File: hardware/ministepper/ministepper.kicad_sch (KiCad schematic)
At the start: 9 parts, among them U1 STM32G071G8U6, U4 SIT3088EEUA

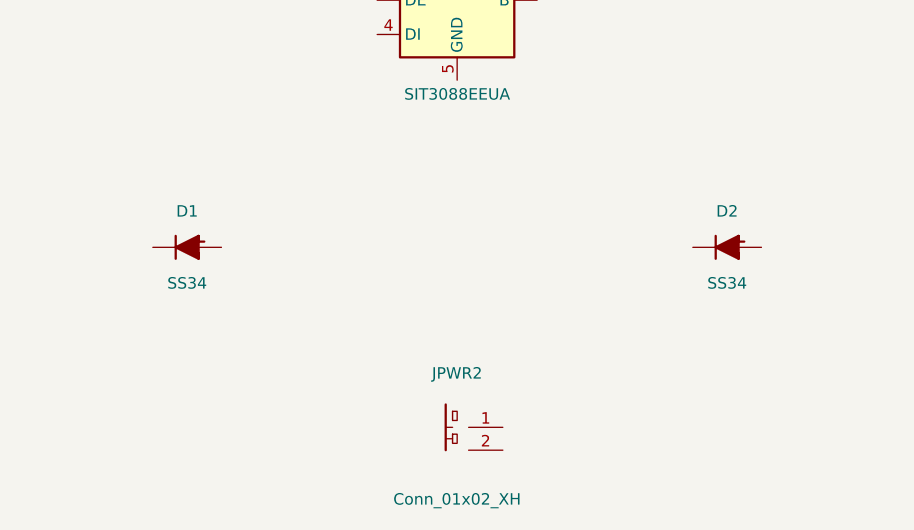
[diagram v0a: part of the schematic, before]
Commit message: hw/ministepper: upgrade D1/D2 SS34 (3A) -> SS54 (5A)
Two TMC2130 drivers at 1.4A continuous each plus chopper peaks and
startup inrush can exceed the SS34's 3A rating on the motor-supply
OR path. SS54 is a drop-in (same SMA footprint, same 40V rating,
JLCPCB basic part C22452) with 5A continuous headroom.

Co-Authored-By: Claude Opus 4.6 (1M context) <noreply@anthropic.com>
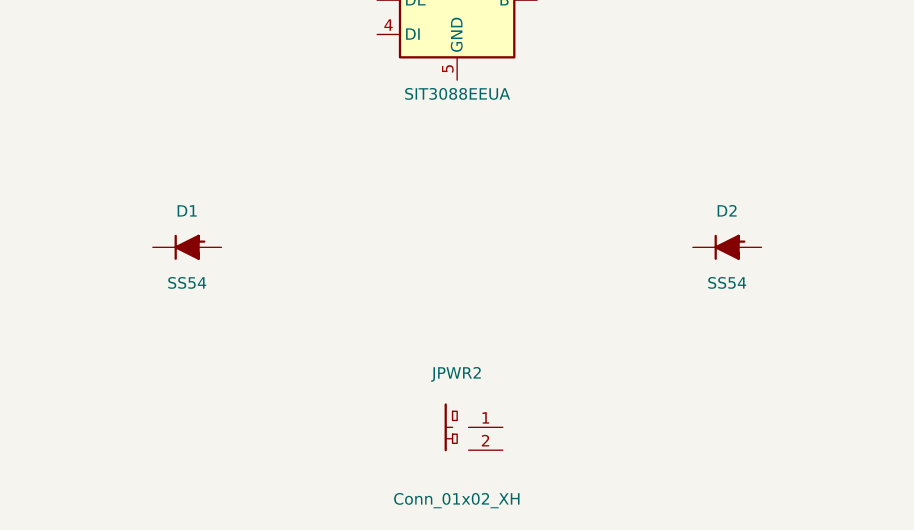
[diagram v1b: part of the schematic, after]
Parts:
- D1, D2: value SS34 -> SS54; LCSC C8678 -> C22452; MPN SS34 -> SS54
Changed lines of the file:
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@@
 			)
 		)
-		(property "Value" "SS34"
+		(property "Value" "SS54"
 			(at 120 214 0)
 			(show_name no)
@@
 			)
 		)
-		(property "Description" "Schottky 3A 40V SMA — reverse-polarity + diode-OR for external motor input (BASIC)"
+		(property "Description" "Schottky 5A 40V SMA — reverse-polarity + diode-OR for external motor input (BASIC)"
 			(at 120 210 0)
 			(hide yes)
@@
 			)
 		)
-		(property "LCSC" "C8678"
+		(property "LCSC" "C22452"
 			(at 120 210 0)
 			(hide yes)
@@
 			)
 		)
-		(property "MPN" "SS34"
+		(property "MPN" "SS54"
 			(at 120 210 0)
 			(hide yes)
@@
 			)
 		)
-		(property "Value" "SS34"
+		(property "Value" "SS54"
 			(at 180 214 0)
 			(show_name no)
@@
 			)
 		)
-		(property "Description" "Schottky 3A 40V SMA — diode-OR from bus V+ onto VPP (BASIC)"
+		(property "Description" "Schottky 5A 40V SMA — diode-OR from bus V+ onto VPP (BASIC)"
 			(at 180 210 0)
 			(hide yes)
@@
 			)
 		)
-		(property "LCSC" "C8678"
+		(property "LCSC" "C22452"
 			(at 180 210 0)
 			(hide yes)
@@
 			)
 		)
-		(property "MPN" "SS34"
+		(property "MPN" "SS54"
 			(at 180 210 0)
 			(hide yes)

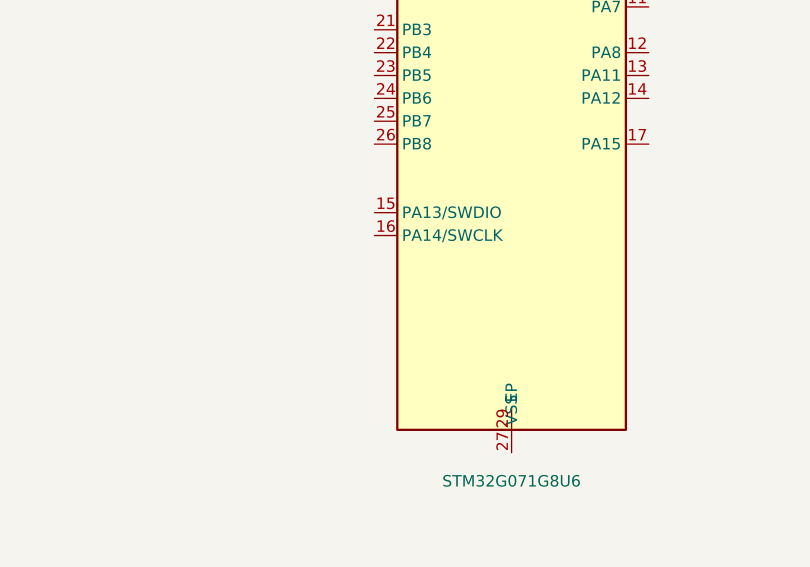
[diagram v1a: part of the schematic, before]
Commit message: hw/ministepper: add BOOT0 pull-down + test pad for bootloader entry
PA14 doubles as SWCLK and the BOOT0 selector (factory default
nBOOT_SEL=1 reads BOOT0 from the pin). Without a pull, PA14 can float
to indeterminate state at cold boot when no debugger is attached and
cause an unintended system-bootloader entry.

- R_BOOT0 (10k 0402, C25744) — locks BOOT0 low at power-up; weak
  enough not to fight SWD drive levels during debug.
- TP_BOOT0 (1x1mm solder pad) — tweezer/pogo to +3V3 at reset to
  invoke the system bootloader over USART2 (RS-485), I2C1 (PB6/PB7),
  or SPI1.

Also embedded Device:R and Connector:TestPoint in lib_symbols so
kicad-cli BOM export recognizes them.

Co-Authored-By: Claude Opus 4.6 (1M context) <noreply@anthropic.com>
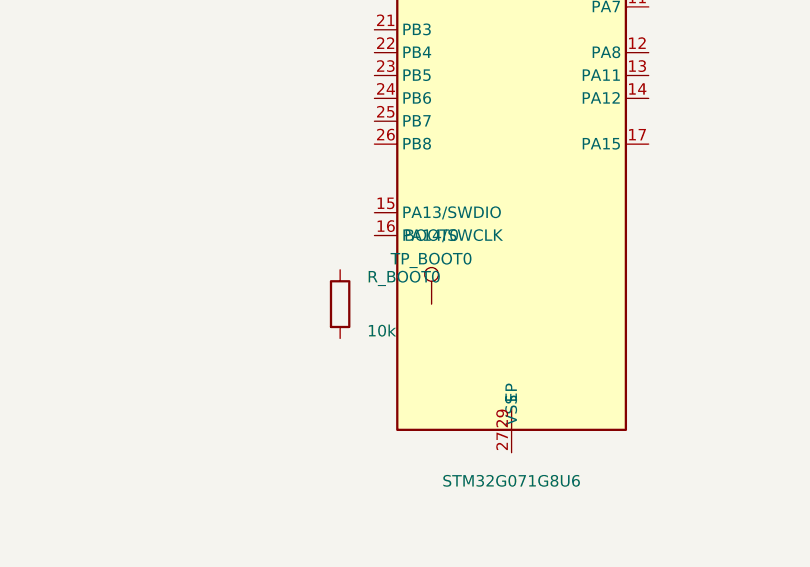
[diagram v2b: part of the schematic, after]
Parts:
- added R_BOOT0: 10k, Resistor_SMD:R_0402_1005Metric, symbol Device:R
- added TP_BOOT0: BOOT0, TestPoint:TestPoint_Pad_1.0x1.0mm, symbol Connector:TestPoint
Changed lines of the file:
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@@
+		)
+	)
+	(symbol
+		(lib_id "Device:R")
+		(at 200.66 134.62 0)
+		(unit 1)
+		(body_style 1)
+		(exclude_from_sim no)
+		(in_bom yes)
+		(on_board yes)
+		(in_pos_files yes)
+		(dnp no)
+		(uuid "b007aa01-1111-2222-3333-00000000r1ab")
+		(property "Reference" "R_BOOT0"
+			(at 203.66 131.62 0)
+			(show_name no)
+			(do_not_autoplace no)
+			(effects
+				(font
+					(size 1.27 1.27)
+				)
+				(justify left)
+			)
+		)
+		(property "Value" "10k"
+			(at 203.66 137.62 0)
+			(show_name no)
+			(do_not_autoplace no)
+			(effects
+				(font
+					(size 1.27 1.27)
+				)
+				(justify left)
+			)
+		)
+		(property "Footprint" "Resistor_SMD:R_0402_1005Metric"
+			(at 200.66 134.62 0)
+			(hide yes)
+			(show_name no)
+			(do_not_autoplace no)
+			(effects
+				(font
+					(size 1.27 1.27)
+				)
+			)
+		)
+		(property "Datasheet" ""
+			(at 200.66 134.62 0)
+			(hide yes)
+			(show_name no)
+			(do_not_autoplace no)
+			(effects
+				(font
+					(size 1.27 1.27)
+				)
+			)
+		)
+		(property "Description" "BOOT0 pull-down on PA14; locks cold boot to flash (BASIC)"
+			(at 200.66 134.62 0)
+			(hide yes)
+			(show_name no)
+			(do_not_autoplace no)
+			(effects
+				(font
+					(size 1.27 1.27)
+				)
+			)
+		)
+		(property "LCSC" "C25744"
+			(at 200.66 134.62 0)
+			(hide yes)
+			(show_name no)
+			(do_not_autoplace no)
+			(effects
+				(font
+					(size 1.27 1.27)
+				)
+			)
+		)
+		(property "MPN" "0402WGF1002TCE"
+			(at 200.66 134.62 0)
+			(hide yes)
+			(show_name no)
+			(do_not_autoplace no)
+			(effects
+				(font
+					(size 1.27 1.27)
+				)
+			)
+		)
+		(property "Manufacturer" "UNI-ROYAL"
+			(at 200.66 134.62 0)
+			(hide yes)
+			(show_name no)
+			(do_not_autoplace no)
+			(effects
+				(font
+					(size 1.27 1.27)
+				)
+			)
+		)
+		(pin "1"
+			(uuid "b007aa01-1111-2222-3333-00000000-pn01")
+		)
+		(pin "2"
+			(uuid "b007aa01-1111-2222-3333-00000000-pn02")
+		)
+		(instances
+			(project "ministepper"
+				(path "/e1d2c3b4-a5f6-7890-abcd-ef9876543210"
+					(reference "R_BOOT0")
+					(unit 1)
+				)
+			)
+		)
+	)
+	(symbol
+		(lib_id "Connector:TestPoint")
+		(at 210.82 134.62 0)
+		(unit 1)
+		(body_style 1)
+		(exclude_from_sim no)
+		(in_bom yes)
+		(on_board yes)
+		(in_pos_files yes)
+		(dnp no)
+		(uuid "b007aa02-1111-2222-3333-00000000tpab")
+		(property "Reference" "TP_BOOT0"
+			(at 210.82 129.62 0)
+			(show_name no)
+			(do_not_autoplace no)
+			(effects
+				(font
+					(size 1.27 1.27)
+				)
+			)
+		)
+		(property "Value" "BOOT0"
+			(at 210.82 127.0 0)
+			(show_name no)
+			(do_not_autoplace no)
+			(effects
+				(font
+					(size 1.27 1.27)
+				)
+			)
+		)
+		(property "Footprint" "TestPoint:TestPoint_Pad_1.0x1.0mm"
+			(at 210.82 134.62 0)
+			(hide yes)
+			(show_name no)
+			(do_not_autoplace no)
+			(effects
+				(font
+					(size 1.27 1.27)
+				)
+			)
+		)
+		(property "Datasheet" ""
+			(at 210.82 134.62 0)
+			(hide yes)
+			(show_name no)
+			(do_not_autoplace no)
+			(effects
+				(font
+					(size 1.27 1.27)
+				)
+			)
+		)
+		(property "Description" "Solder test point for manual BOOT0 select (short to +3V3 at reset)"
+			(at 210.82 134.62 0)
+			(hide yes)
+			(show_name no)
+			(do_not_autoplace no)
+			(effects
+				(font
+					(size 1.27 1.27)
+				)
+			)
+		)
+		(pin "1"
+			(uuid "b007aa02-1111-2222-3333-00000000-pn01")
+		)
+		(instances
+			(project "ministepper"
+				(path "/e1d2c3b4-a5f6-7890-abcd-ef9876543210"
+					(reference "TP_BOOT0")
+					(unit 1)
+				)
+			)
 		)
 	)

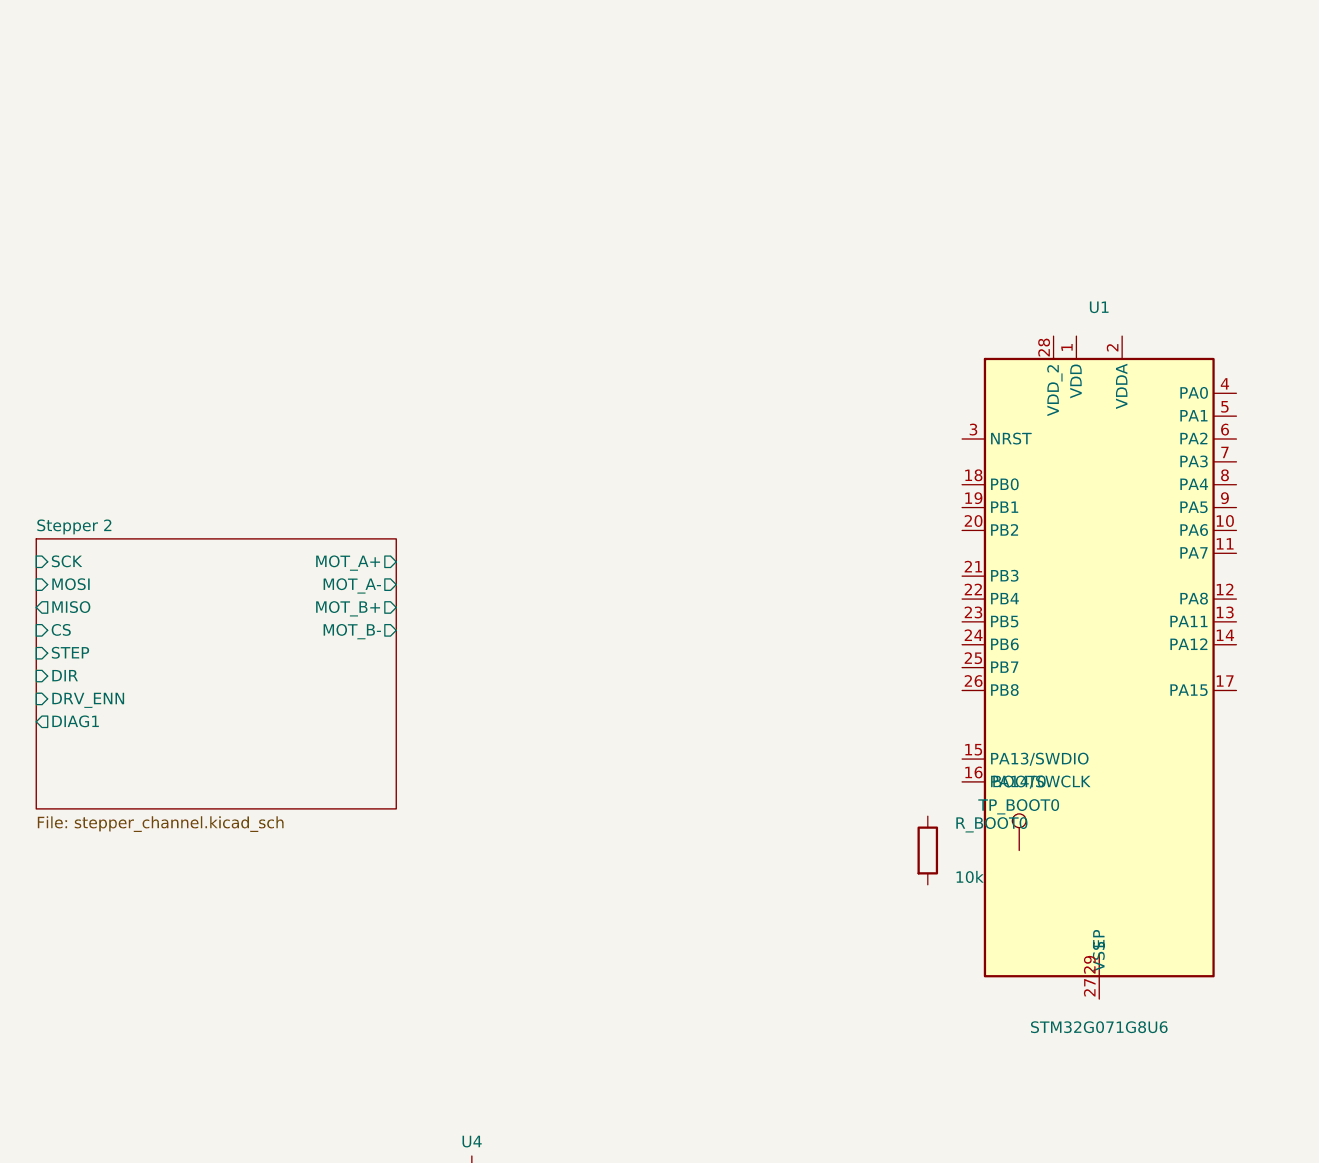
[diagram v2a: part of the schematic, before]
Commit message: hw: fix STM32G071G8U6 symbol — EP pin 29 overlapped VSS pin 27
Both pins were placed at x=0 on the bottom edge (VSS at y=-36.83, EP
at y=-34.29). With 2.54mm pin-body length drawn inward, VSS's tip
landed exactly at EP's base, producing overlapping pin lines on the
bottom of the symbol.

Moved EP to (5.08, -36.83) on the same bottom edge, offset right of
VSS. Patched the master in lib/symbols/tsumikoro.kicad_sym and the
embedded copy in ministepper.kicad_sch.

Co-Authored-By: Claude Opus 4.6 (1M context) <noreply@anthropic.com>
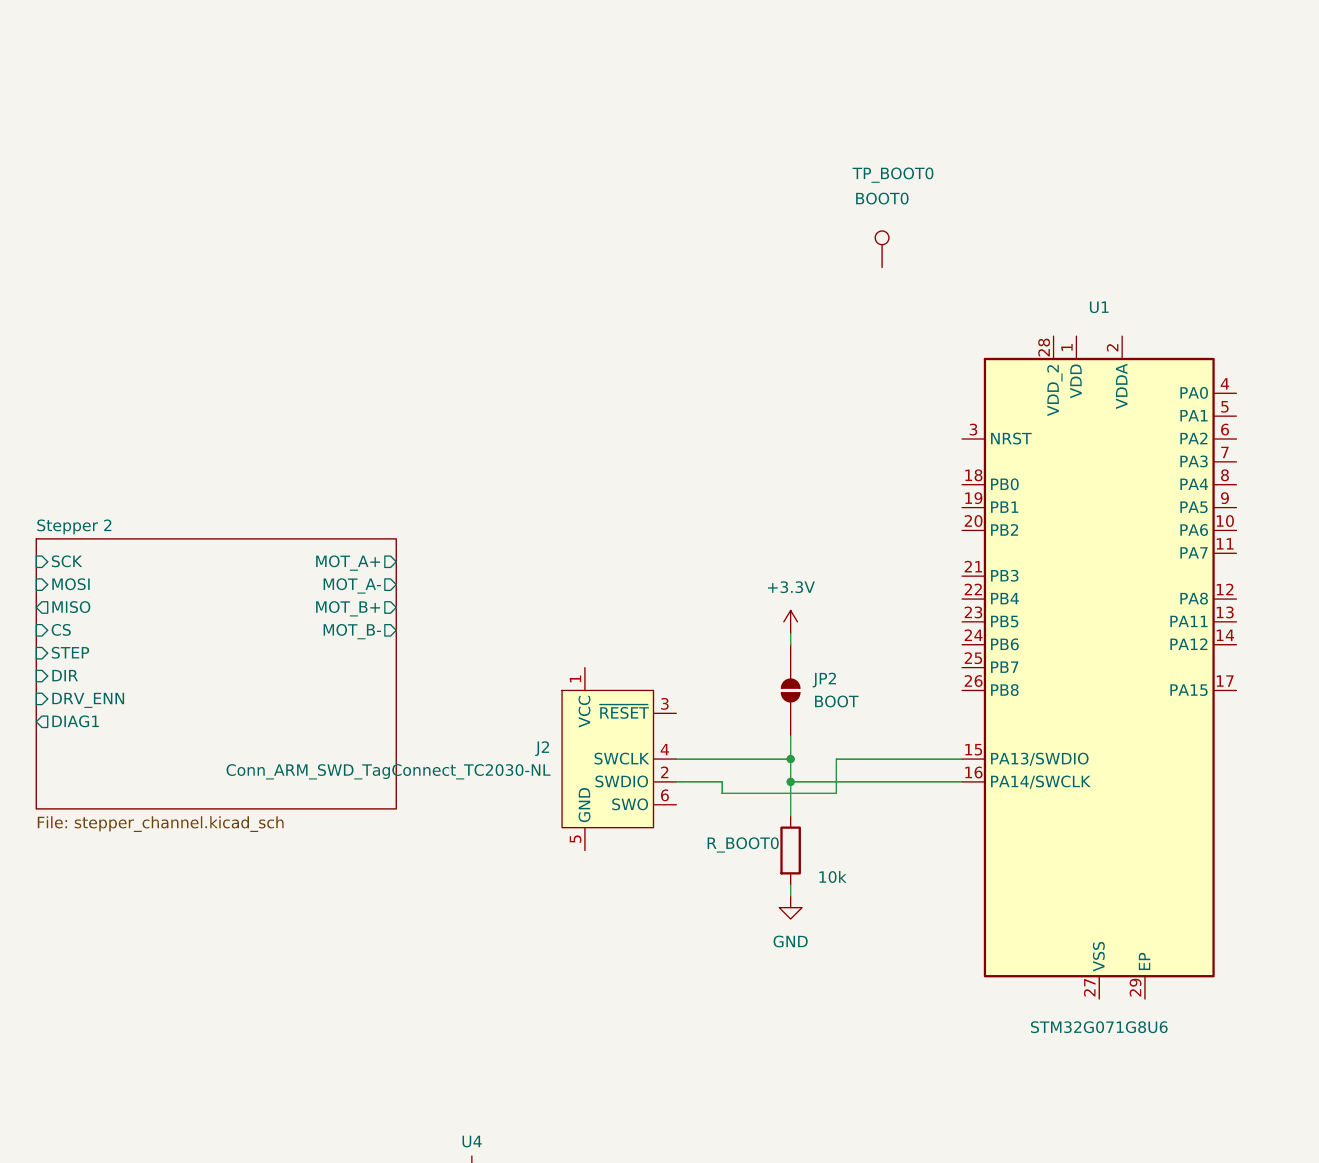
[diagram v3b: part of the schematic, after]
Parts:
- added J2: Conn_ARM_SWD_TagConnect_TC2030-NL, Connector:Tag-Connect_TC2030-IDC-NL_2x03_P1.27mm_Vertical, symbol Connector:Conn_ARM_SWD_TagConnect_TC2030-NL
- added JP2: BOOT, Jumper:SolderJumper-2_P1.3mm_Open_Pad1.0x1.5mm, symbol Jumper:SolderJumper_2_Open
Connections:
- net at U1.15 (PA13/SWDIO): now also J2.2 (SWDIO)
- net at U1.16 (PA14/SWCLK): now also R_BOOT0.1, J2.4 (SWCLK), JP2.1 (A)
- net GND: now reaches R_BOOT0.2
- new net +3.3V: JP2.2 (B)
